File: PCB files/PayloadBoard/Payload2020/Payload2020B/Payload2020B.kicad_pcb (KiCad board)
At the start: 2 copper layers, 38.1 x 127 mm, 3 parts, among them J1 BridgeConn, U1 Xbee_XBP9B, U2 BerryIMUv3

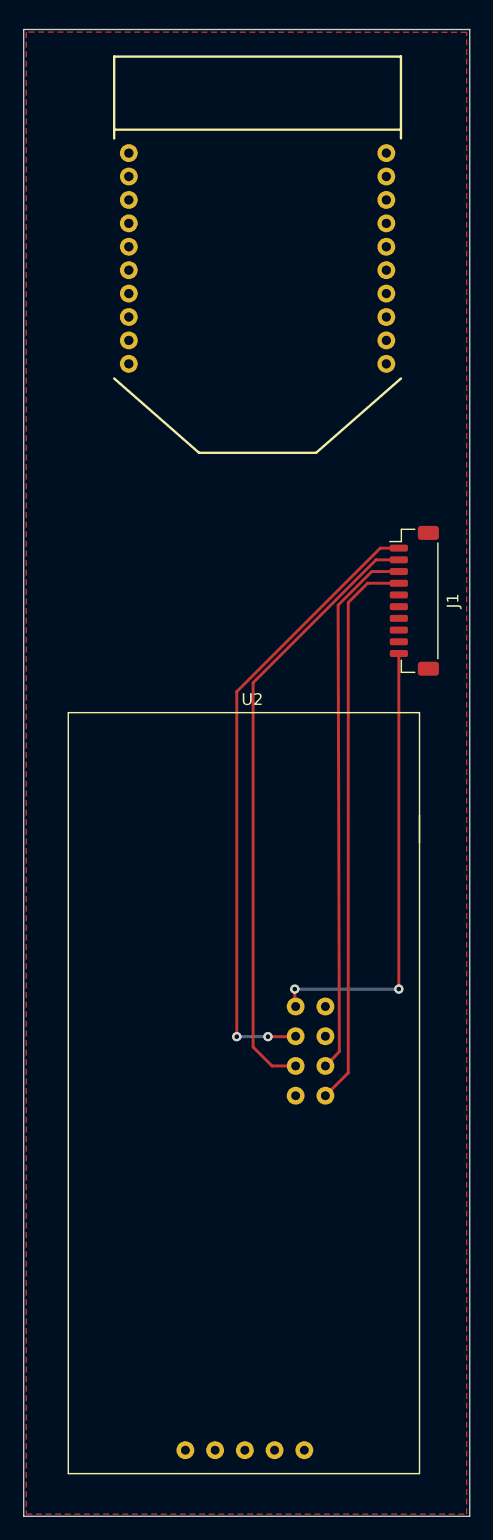
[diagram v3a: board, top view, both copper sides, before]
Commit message: Placed corner mounting holes on each board Drew backside ground plane on Board B
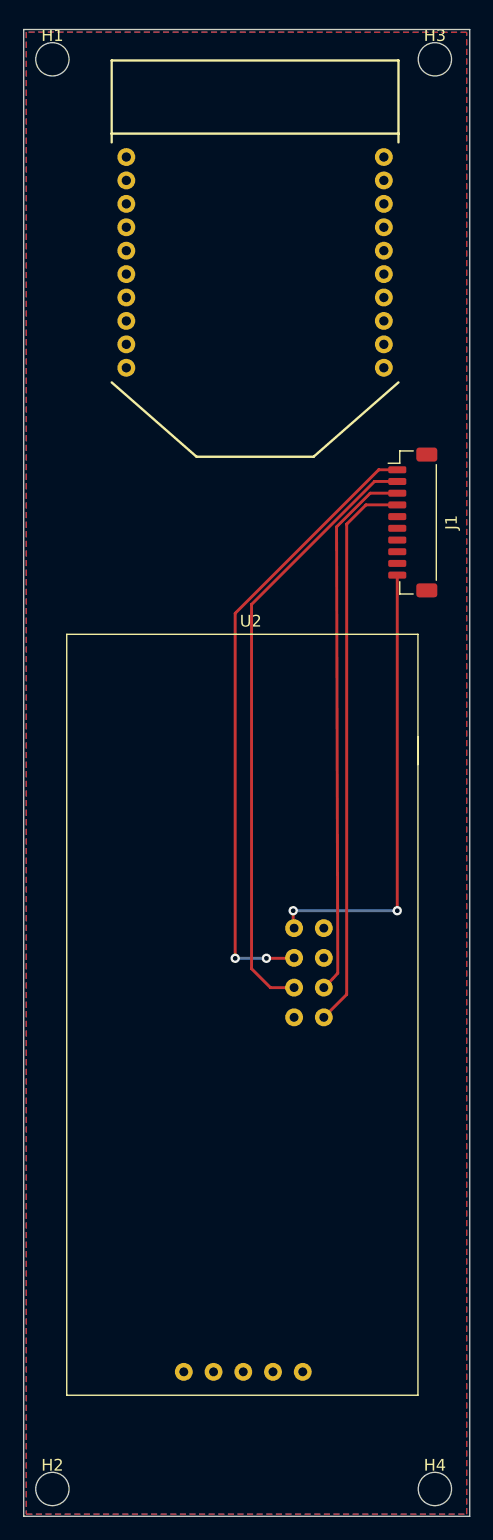
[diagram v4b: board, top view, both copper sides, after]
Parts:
- added H1: Corner, Payload:MountingHole_4-40, F.Cu at (122.3, 34.2)
- added H2: Corner, Payload:MountingHole_4-40, F.Cu at (122.3, 156.4)
- added H3: Corner, Payload:MountingHole_4-40, F.Cu at (155.0, 34.2)
- added H4: Corner, Payload:MountingHole_4-40, F.Cu at (155.0, 156.4)
- moved J1 6.69 mm to (153.1, 73.8)
- moved U2 6.69 mm to (139.4, 117.3)
- moved U1 0.40 mm to (139.6, 40.6)
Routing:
- added copper zone on B.Cu, net GNDREF
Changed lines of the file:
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@@
-(kicad_pcb (version 20171130) (host pcbnew 5.1.5-52549c5~84~ubuntu18.04.1)
+(kicad_pcb (version 20171130) (host pcbnew "(5.1.2)-2")
   (general
     (thickness 1.6)
-    (drawings 4)
+    (drawings 5)
     (tracks 29)
     (zones 0)
-    (modules 3)
+    (modules 7)
     (nets 28)
   )
@@
   )
   (module Payload:BerryGPS-IMU_V3 (layer F.Cu)
-    (at 139.55014 124.0282)
+    (at 139.41552 117.3353)
     (fp_text reference U2 (at -0.17272 -35.09772) (layer F.SilkS)
       (effects (font (size 1 1) (thickness 0.15)))
@@
   )
   (module SparkFunRF:XBEE-1 (layer F.Cu)
-    (at 139.827 40.259 180)
+    (at 139.61364 40.59428 180)
     (attr virtual)
     (fp_text reference U1 (at -7.874 -2.7432) (layer B.SilkS)
@@
   )
   (module Connector_JST:JST_SH_BM10B-SRSS-TB_1x10-1MP_P1.00mm_Vertical (layer F.Cu)
-    (at 153.21788 80.50022 270)
+    (at 153.08326 73.80732 270)
     (descr "JST SH series connector, BM10B-SRSS-TB (http://www.jst-mfg.com/product/pdf/eng/eSH.pdf), generated with kicad-footprint-generator")
     (tags "connector JST SH side entry")
@@
     )
   )
+  (module Payload:MountingHole_4-40 (layer F.Cu)
+    (at 122.301 34.24682)
+    (fp_text reference H1 (at 0 -2.032) (layer F.SilkS)
+      (effects (font (size 1 1) (thickness 0.15)))
+    )
+    (fp_text value Corner (at 0 2.286) (layer F.Fab)
+      (effects (font (size 1 1) (thickness 0.15)))
+    )
+    (pad "" np_thru_hole circle (at 0 0) (size 2.8448 2.8448) (drill 2.8448) (layers *.Cu *.Mask))
+  )
+  (module Payload:MountingHole_4-40 (layer F.Cu)
+    (at 122.301 156.36748)
+    (fp_text reference H2 (at 0 -2.032) (layer F.SilkS)
+      (effects (font (size 1 1) (thickness 0.15)))
+    )
+    (fp_text value Corner (at 0 2.286) (layer F.Fab)
+      (effects (font (size 1 1) (thickness 0.15)))
+    )
+    (pad "" np_thru_hole circle (at 0 0) (size 2.8448 2.8448) (drill 2.8448) (layers *.Cu *.Mask))
+  )
+  (module Payload:MountingHole_4-40 (layer F.Cu)
+    (at 154.97302 34.24682)
+    (fp_text reference H3 (at 0 -2.032) (layer F.SilkS)
+      (effects (font (size 1 1) (thickness 0.15)))
+    )
+    (fp_text value Corner (at 0 2.286) (layer F.Fab)
+      (effects (font (size 1 1) (thickness 0.15)))
+    )
+    (pad "" np_thru_hole circle (at 0 0) (size 2.8448 2.8448) (drill 2.8448) (layers *.Cu *.Mask))
+  )
+  (module Payload:MountingHole_4-40 (layer F.Cu)
+    (at 154.97302 156.36748)
+    (fp_text reference H4 (at 0 -2.032) (layer F.SilkS)
+      (effects (font (size 1 1) (thickness 0.15)))
+    )
+    (fp_text value Corner (at 0 2.286) (layer F.Fab)
+      (effects (font (size 1 1) (thickness 0.15)))
+    )
+    (pad "" np_thru_hole circle (at 0 0) (size 2.8448 2.8448) (drill 2.8448) (layers *.Cu *.Mask))
+  )
+  (gr_line (start 179.55514 63) (end 179.55514 63.239) (layer Dwgs.User) (width 0.15))
   (gr_line (start 119.85014 31.6992) (end 119.85014 158.6992) (layer Edge.Cuts) (width 0.05))
   (gr_line (start 157.95014 158.6992) (end 157.95014 31.6992) (layer Edge.Cuts) (width 0.05))
   (gr_line (start 119.85014 158.6992) (end 157.95014 158.6992) (layer Edge.Cuts) (width 0.05))
   (gr_line (start 119.85014 31.6992) (end 157.95014 31.6992) (layer Edge.Cuts) (width 0.05))
-  (segment (start 138.049 88.260046) (end 138.049 117.729) (width 0.25) (layer F.Cu) (net 1))
-  (via (at 138.049 117.729) (size 0.8) (drill 0.4) (layers F.Cu B.Cu) (net 1))
-  (segment (start 151.89288 76.00022) (end 150.308826 76.00022) (width 0.25) (layer F.Cu) (net 1))
-  (segment (start 150.308826 76.00022) (end 138.049 88.260046) (width 0.25) (layer F.Cu) (net 1))
-  (via (at 140.716 117.729) (size 0.8) (drill 0.4) (layers F.Cu B.Cu) (net 1))
-  (segment (start 138.049 117.729) (end 140.716 117.729) (width 0.25) (layer B.Cu) (net 1))
-  (segment (start 143.04406 117.729) (end 143.0799 117.69316) (width 0.25) (layer F.Cu) (net 1))
-  (segment (start 140.716 117.729) (end 143.04406 117.729) (width 0.25) (layer F.Cu) (net 1))
-  (segment (start 149.945236 77.00022) (end 139.446 87.499456) (width 0.25) (layer F.Cu) (net 2))
-  (segment (start 151.89288 77.00022) (end 149.945236 77.00022) (width 0.25) (layer F.Cu) (net 2))
-  (segment (start 139.446 87.499456) (end 139.446 118.618) (width 0.25) (layer F.Cu) (net 2))
-  (segment (start 141.06116 120.23316) (end 143.0799 120.23316) (width 0.25) (layer F.Cu) (net 2))
-  (segment (start 139.446 118.618) (end 141.06116 120.23316) (width 0.25) (layer F.Cu) (net 2))
-  (segment (start 146.381899 119.471161) (end 145.6199 120.23316) (width 0.25) (layer F.Cu) (net 3))
-  (segment (start 146.812 118.999) (end 146.381899 119.471161) (width 0.25) (layer F.Cu) (net 3))
-  (segment (start 146.706901 80.875689) (end 146.812 118.999) (width 0.25) (layer F.Cu) (net 3))
-  (segment (start 151.89288 78.00022) (end 149.58237 78.00022) (width 0.25) (layer F.Cu) (net 3))
-  (segment (start 149.58237 78.00022) (end 146.706901 80.875689) (width 0.25) (layer F.Cu) (net 3))
-  (segment (start 147.574 120.81906) (end 145.6199 122.77316) (width 0.25) (layer F.Cu) (net 4))
-  (segment (start 147.574 80.645) (end 147.574 120.81906) (width 0.25) (layer F.Cu) (net 4))
-  (segment (start 149.21878 79.00022) (end 147.574 80.645) (width 0.25) (layer F.Cu) (net 4))
-  (segment (start 151.89288 79.00022) (end 149.21878 79.00022) (width 0.25) (layer F.Cu) (net 4))
-  (via (at 151.892 113.665) (size 0.8) (drill 0.4) (layers F.Cu B.Cu) (net 27))
-  (segment (start 151.89288 85.00022) (end 151.89288 113.66412) (width 0.25) (layer F.Cu) (net 27))
-  (segment (start 151.89288 113.66412) (end 151.892 113.665) (width 0.25) (layer F.Cu) (net 27))
-  (via (at 143.002 113.665) (size 0.8) (drill 0.4) (layers F.Cu B.Cu) (net 27))
-  (segment (start 151.892 113.665) (end 143.002 113.665) (width 0.25) (layer B.Cu) (net 27))
-  (segment (start 143.002 115.07526) (end 143.0799 115.15316) (width 0.25) (layer F.Cu) (net 27))
-  (segment (start 143.002 113.665) (end 143.002 115.07526) (width 0.25) (layer F.Cu) (net 27))
+  (segment (start 137.91438 81.567146) (end 137.91438 111.0361) (width 0.25) (layer F.Cu) (net 1))
+  (via (at 137.91438 111.0361) (size 0.8) (drill 0.4) (layers F.Cu B.Cu) (net 1))
+  (segment (start 151.75826 69.30732) (end 150.174206 69.30732) (width 0.25) (layer F.Cu) (net 1))
+  (segment (start 150.174206 69.30732) (end 137.91438 81.567146) (width 0.25) (layer F.Cu) (net 1))
+  (via (at 140.58138 111.0361) (size 0.8) (drill 0.4) (layers F.Cu B.Cu) (net 1))
+  (segment (start 137.91438 111.0361) (end 140.58138 111.0361) (width 0.25) (layer B.Cu) (net 1))
+  (segment (start 142.90944 111.0361) (end 142.94528 111.00026) (width 0.25) (layer F.Cu) (net 1))
+  (segment (start 140.58138 111.0361) (end 142.90944 111.0361) (width 0.25) (layer F.Cu) (net 1))
+  (segment (start 149.810616 70.30732) (end 139.31138 80.806556) (width 0.25) (layer F.Cu) (net 2))
+  (segment (start 151.75826 70.30732) (end 149.810616 70.30732) (width 0.25) (layer F.Cu) (net 2))
+  (segment (start 139.31138 80.806556) (end 139.31138 111.9251) (width 0.25) (layer F.Cu) (net 2))
+  (segment (start 140.92654 113.54026) (end 142.94528 113.54026) (width 0.25) (layer F.Cu) (net 2))
+  (segment (start 139.31138 111.9251) (end 140.92654 113.54026) (width 0.25) (layer F.Cu) (net 2))
+  (segment (start 146.247279 112.778261) (end 145.48528 113.54026) (width 0.25) (layer F.Cu) (net 3))
+  (segment (start 146.67738 112.3061) (end 146.247279 112.778261) (width 0.25) (layer F.Cu) (net 3))
+  (segment (start 146.572281 74.182789) (end 146.67738 112.3061) (width 0.25) (layer F.Cu) (net 3))
+  (segment (start 151.75826 71.30732) (end 149.44775 71.30732) (width 0.25) (layer F.Cu) (net 3))
+  (segment (start 149.44775 71.30732) (end 146.572281 74.182789) (width 0.25) (layer F.Cu) (net 3))
+  (segment (start 147.43938 114.12616) (end 145.48528 116.08026) (width 0.25) (layer F.Cu) (net 4))
+  (segment (start 147.43938 73.9521) (end 147.43938 114.12616) (width 0.25) (layer F.Cu) (net 4))
+  (segment (start 149.08416 72.30732) (end 147.43938 73.9521) (width 0.25) (layer F.Cu) (net 4))
+  (segment (start 151.75826 72.30732) (end 149.08416 72.30732) (width 0.25) (layer F.Cu) (net 4))
+  (via (at 151.75738 106.9721) (size 0.8) (drill 0.4) (layers F.Cu B.Cu) (net 27))
+  (segment (start 151.75826 78.30732) (end 151.75826 106.97122) (width 0.25) (layer F.Cu) (net 27))
+  (segment (start 151.75826 106.97122) (end 151.75738 106.9721) (width 0.25) (layer F.Cu) (net 27))
+  (via (at 142.86738 106.9721) (size 0.8) (drill 0.4) (layers F.Cu B.Cu) (net 27))
+  (segment (start 151.75738 106.9721) (end 142.86738 106.9721) (width 0.25) (layer B.Cu) (net 27))
+  (segment (start 142.86738 108.38236) (end 142.94528 108.46026) (width 0.25) (layer F.Cu) (net 27))
+  (segment (start 142.86738 106.9721) (end 142.86738 108.38236) (width 0.25) (layer F.Cu) (net 27))
   (zone (net 16) (net_name GNDREF) (layer F.Cu) (hatch edge 0.508)
     (connect_pads (clearance 0.508))
@@
       )
     )
+  )
+  (zone (net 16) (net_name GNDREF) (layer B.Cu) (hatch edge 0.508)
+    (connect_pads (clearance 0.508))
+    (min_thickness 0.254)
+    (fill (arc_segments 32) (thermal_gap 0.508) (thermal_bridge_width 0.508))
+    (polygon
+      (pts
+        (xy 157.6832 31.9405) (xy 120.07088 31.92018) (xy 120.07088 158.51378) (xy 157.68574 158.51378) (xy 157.68574 31.9405)
+      )
+    )

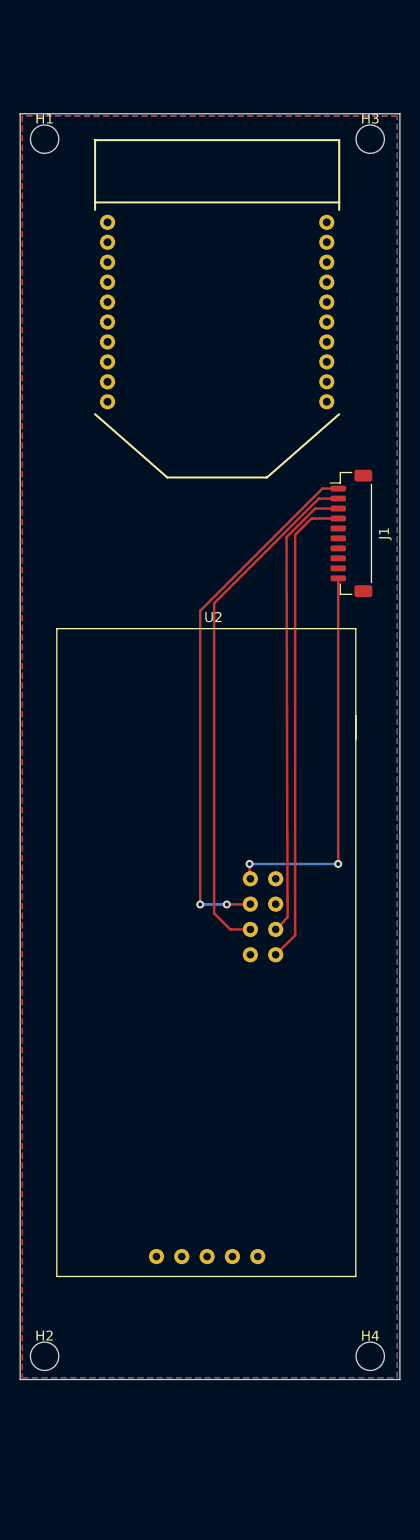
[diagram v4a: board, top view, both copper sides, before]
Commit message: Redrawn edge cuts for board B Redrawn GND planes Changed bridge connector to molex picoblade
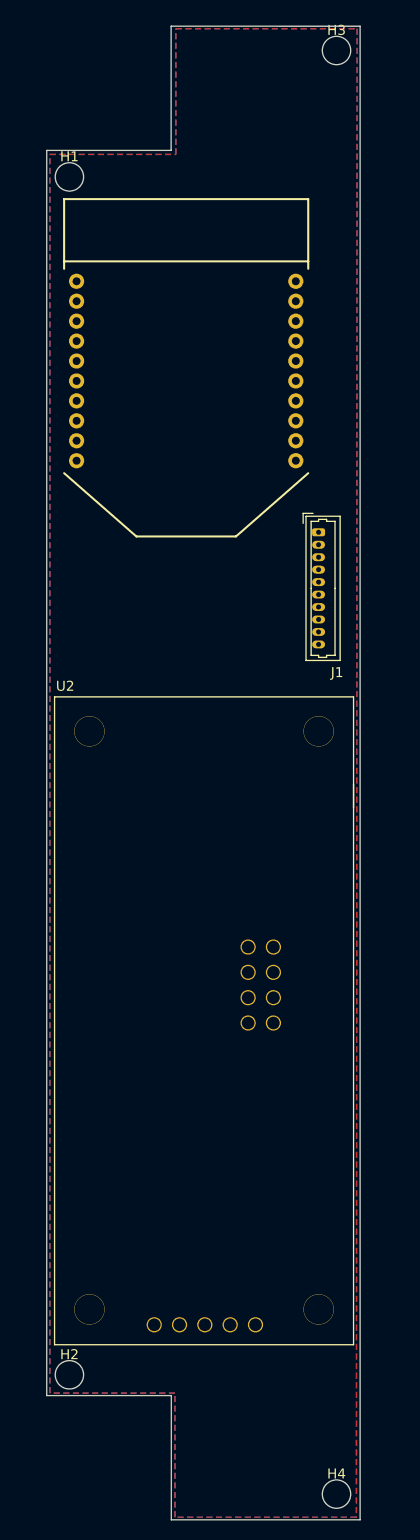
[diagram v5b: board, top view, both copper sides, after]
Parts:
- J1: footprint Connector_JST:JST_SH_BM10B-SRSS-TB_1x10-1MP_P1.00mm_Vertical -> Connector_Molex:Molex_PicoBlade_53047-1010_1x10_P1.25mm_Vertical
- moved U2 31.5 mm to (123.3, 90.2)
- moved H4 14.2 mm to (151.6, 170.2)
- moved H3 9.52 mm to (151.6, 25.4)
- moved U1 6.68 mm to (136.5, 46.5)
- moved H1 4.53 mm to (124.8, 38.0)
- moved J1 3.29 mm to (149.8, 73.7)
- moved H2 3.11 mm to (124.8, 158.2)
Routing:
- net /Berry_SDA: track 53.4 -> 0.00 mm, vias 2 -> 0
- net /Berry_SCL: track 52.2 -> 0.00 mm
- net /TX_GPS: track 47.9 -> 0.00 mm
- net /RX_GPS: track 46.2 -> 0.00 mm
- net +3V3: track 39.1 -> 0.00 mm, vias 2 -> 0
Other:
- board size 38.1 x 127 mm -> 31.4 x 149.9 mm

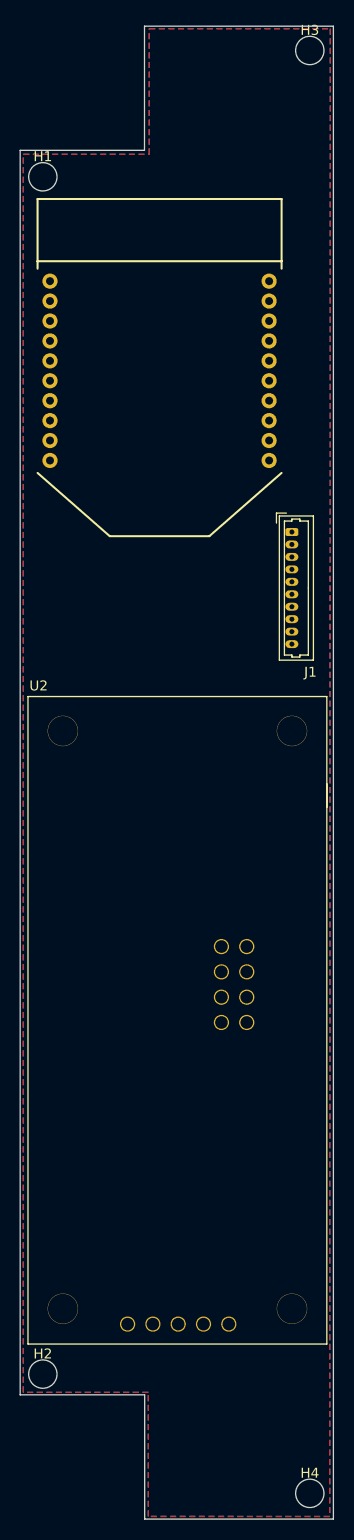
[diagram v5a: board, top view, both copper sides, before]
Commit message: BIG changus -Fully routed both boards -Changed board to board connector to JST SH -Changed load cell connector to molex picoblade -Added silkscreen version & signature -Moved arducam connector to align with payload structure
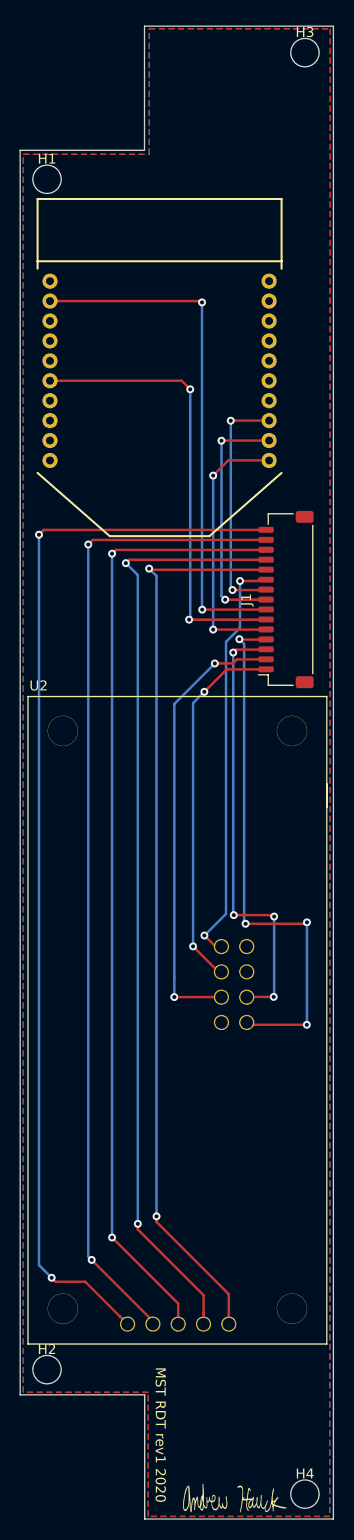
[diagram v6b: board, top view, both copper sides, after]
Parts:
- added G***: LOGO, Board images:AAHsig, F.Cu at (144.0, 170.8)
- J1: footprint Connector_Molex:Molex_PicoBlade_53047-1010_1x10_P1.25mm_Vertical -> Connector_JST:JST_SH_SM15B-SRSS-TB_1x15-1MP_P1.00mm_Horizontal
- moved J1 6.80 mm to (149.2, 80.5), turned to 90 degrees
- moved H2 0.61 mm to (125.2, 157.8)
- moved H3 0.53 mm to (151.1, 25.6)
- moved H4 0.49 mm to (151.1, 170.3)
- moved H1 0.49 mm to (125.2, 38.3)
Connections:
- U2 pad 2: Net-(U2-Pad2) -> /Berry_SDA
- U2 pad 3: /Berry_SDA -> /Berry_SCL
- U2 pad 4: GNDREF -> Net-(U2-Pad4)
- U2 pad 5: /Berry_SCL -> Net-(U2-Pad5)
- U2 pad 6: /RX_GPS -> GNDREF
- U2 pad 7: Net-(U2-Pad7) -> /RX_GPS
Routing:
- net Net-(J1-Pad15): track 0.00 -> 107.0 mm, vias 0 -> 2
- net Net-(J1-Pad14): track 0.00 -> 98.3 mm, vias 0 -> 2
- net Net-(J1-Pad13): track 0.00 -> 95.0 mm, vias 0 -> 2
- net Net-(J1-Pad12): track 0.00 -> 93.2 mm, vias 0 -> 2
- net Net-(J1-Pad11): track 0.00 -> 90.3 mm, vias 0 -> 2
- net /TX_GPS: track 0.00 -> 53.5 mm, vias 0 -> 4
- net /XBEE_CTS: track 0.00 -> 51.9 mm, vias 0 -> 2
- net /XBEE_RTS: track 0.00 -> 44.7 mm, vias 0 -> 2
- net /Berry_SCL: track 0.00 -> 44.5 mm, vias 0 -> 2
- net /RX_GPS: track 0.00 -> 44.0 mm, vias 0 -> 4
- net +3V3: track 0.00 -> 41.2 mm, vias 0 -> 2
- net /Berry_SDA: track 0.00 -> 36.4 mm, vias 0 -> 2
- net +3.3VA: track 0.00 -> 26.3 mm, vias 0 -> 2
- net /XBEE_DOUT: track 0.00 -> 24.3 mm, vias 0 -> 2
- net /XBEE_DIN: track 0.00 -> 23.7 mm, vias 0 -> 2
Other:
- net class Default: trace_width 0.25 -> 0.24892; via_dia 0.8 -> 0.8001; via_drill 0.4 -> 0.39878
- rule trace_min: 0.2 -> 0.0889
- rule via_min_drill: 0.3 -> 0.254
- rule via_min_size: 0.4 -> 0.4572
- board text added: "MST RDT rev1 2020"
